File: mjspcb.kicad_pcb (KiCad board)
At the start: 2 copper layers, 97.2 x 55.9 mm, 78 parts, among them P1 Batteries, P10 Lipo, P2 serial breakout, P3 I2C breakout, P4 GPS, P5 piezo, P6 BPW34, P7 electrodes, P8 perfboard breakout, P9 reset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

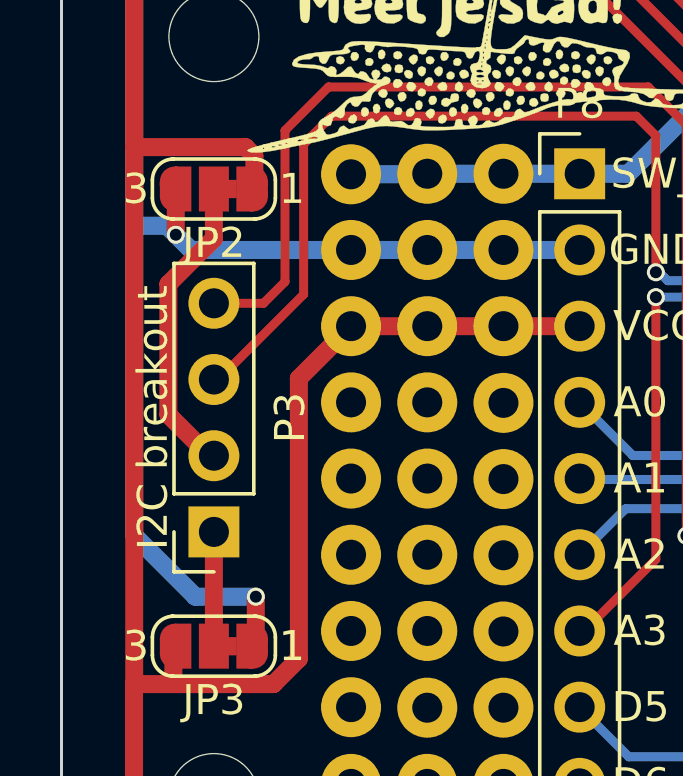
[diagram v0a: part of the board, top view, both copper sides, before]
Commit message: Flip I²C socket
This swaps the pin numbering, to match the Grove pinout. The PCB layout
is also updated to flip the footprint, and move a few traces to make
room for the square pad on the other side.
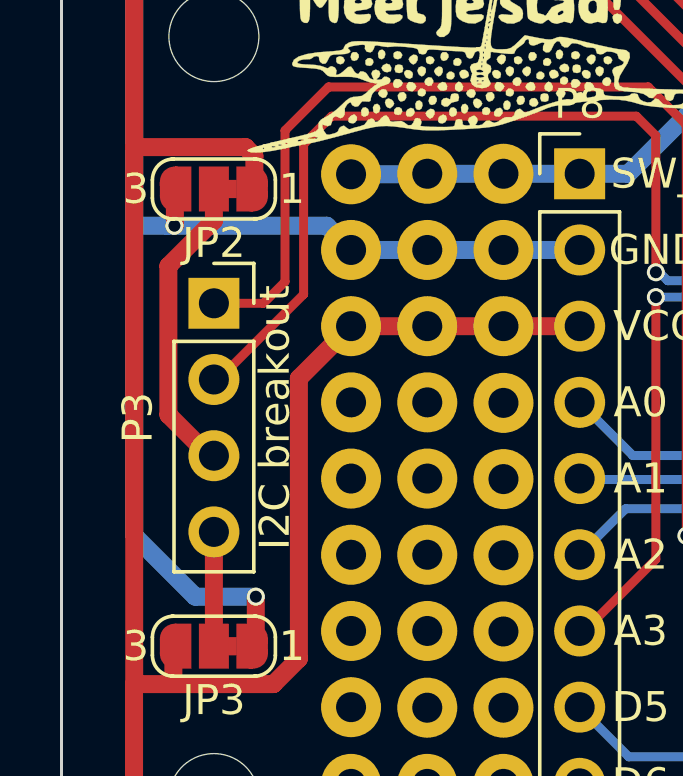
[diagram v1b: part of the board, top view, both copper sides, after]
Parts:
- moved P3 7.62 mm to (139.7, 116.8), turned to 0 degrees
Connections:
- P3 pad 1: Net-(JP3-Pad2) -> SCL
- P3 pad 2: Net-(JP2-Pad2) -> SDA
- P3 pad 3: SDA -> Net-(JP2-Pad2)
- P3 pad 4: SCL -> Net-(JP3-Pad2)
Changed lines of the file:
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@@
     (thickness 1.6)
     (drawings 35)
-    (tracks 533)
+    (tracks 534)
     (zones 0)
     (modules 78)
@@
     (add_net VIN)
   )
+  (module Connector_PinSocket_2.54mm:PinSocket_1x04_P2.54mm_Vertical (layer F.Cu)
+    (at 139.7 116.84)
+    (descr "Through hole straight socket strip, 1x04, 2.54mm pitch, single row (from Kicad 4.0.7), script generated")
+    (tags "Through hole socket strip THT 1x04 2.54mm single row")
+    (fp_text reference P3 (at -2.54 3.81 90) (layer F.SilkS)
+      (effects (font (size 1 1) (thickness 0.15)))
+    )
+    (fp_text value "I2C breakout" (at 2.032 3.81 90) (layer F.SilkS)
+      (effects (font (size 1 1) (thickness 0.15)))
+    )
+    (fp_line (start -1.27 -1.27) (end 0.635 -1.27) (layer F.Fab) (width 0.1))
+    (fp_line (start 0.635 -1.27) (end 1.27 -0.635) (layer F.Fab) (width 0.1))
+    (fp_line (start 1.27 -0.635) (end 1.27 8.89) (layer F.Fab) (width 0.1))
+    (fp_line (start 1.27 8.89) (end -1.27 8.89) (layer F.Fab) (width 0.1))
+    (fp_line (start -1.27 8.89) (end -1.27 -1.27) (layer F.Fab) (width 0.1))
+    (fp_line (start -1.33 1.27) (end 1.33 1.27) (layer F.SilkS) (width 0.12))
+    (fp_line (start -1.33 1.27) (end -1.33 8.95) (layer F.SilkS) (width 0.12))
+    (fp_line (start -1.33 8.95) (end 1.33 8.95) (layer F.SilkS) (width 0.12))
+    (fp_line (start 1.33 1.27) (end 1.33 8.95) (layer F.SilkS) (width 0.12))
+    (fp_line (start 1.33 -1.33) (end 1.33 0) (layer F.SilkS) (width 0.12))
+    (fp_line (start 0 -1.33) (end 1.33 -1.33) (layer F.SilkS) (width 0.12))
+    (fp_line (start -1.8 -1.8) (end 1.75 -1.8) (layer F.CrtYd) (width 0.05))
+    (fp_line (start 1.75 -1.8) (end 1.75 9.4) (layer F.CrtYd) (width 0.05))
+    (fp_line (start 1.75 9.4) (end -1.8 9.4) (layer F.CrtYd) (width 0.05))
+    (fp_line (start -1.8 9.4) (end -1.8 -1.8) (layer F.CrtYd) (width 0.05))
+    (fp_text user %R (at 0 3.81 90) (layer F.Fab)
+      (effects (font (size 1 1) (thickness 0.15)))
+    )
+    (pad 1 thru_hole rect (at 0 0) (size 1.7 1.7) (drill 1) (layers *.Cu *.Mask)
+      (net 11 SCL))
+    (pad 2 thru_hole oval (at 0 2.54) (size 1.7 1.7) (drill 1) (layers *.Cu *.Mask)
+      (net 10 SDA))
+    (pad 3 thru_hole oval (at 0 5.08) (size 1.7 1.7) (drill 1) (layers *.Cu *.Mask)
+      (net 42 "Net-(JP2-Pad2)"))
+    (pad 4 thru_hole oval (at 0 7.62) (size 1.7 1.7) (drill 1) (layers *.Cu *.Mask)
+      (net 43 "Net-(JP3-Pad2)"))
+    (model ${KISYS3DMOD}/Connector_PinSocket_2.54mm.3dshapes/PinSocket_1x04_P2.54mm_Vertical.wrl
+      (at (xyz 0 0 0))
+      (scale (xyz 1 1 1))
+      (rotate (xyz 0 0 0))
+    )
+  )
   (module meetjestad:SolderJumper-3_P1.3mm_Bridged12_RoundedPad1.0x1.5mm_NumberLabels (layer F.Cu)
     (at 139.7 128.27 180)
@@
     )
   )
-  (module Connector_PinSocket_2.54mm:PinSocket_1x04_P2.54mm_Vertical (layer F.Cu)
-    (at 139.7 124.46 180)
-    (descr "Through hole straight socket strip, 1x04, 2.54mm pitch, single row (from Kicad 4.0.7), script generated")
-    (tags "Through hole socket strip THT 1x04 2.54mm single row")
-    (fp_text reference P3 (at -2.54 3.81 270) (layer F.SilkS)
-      (effects (font (size 1 1) (thickness 0.15)))
-    )
-    (fp_text value "I2C breakout" (at 2.032 3.81 270) (layer F.SilkS)
-      (effects (font (size 1 1) (thickness 0.15)))
-    )
-    (fp_line (start -1.27 -1.27) (end 0.635 -1.27) (layer F.Fab) (width 0.1))
-    (fp_line (start 0.635 -1.27) (end 1.27 -0.635) (layer F.Fab) (width 0.1))
-    (fp_line (start 1.27 -0.635) (end 1.27 8.89) (layer F.Fab) (width 0.1))
-    (fp_line (start 1.27 8.89) (end -1.27 8.89) (layer F.Fab) (width 0.1))
-    (fp_line (start -1.27 8.89) (end -1.27 -1.27) (layer F.Fab) (width 0.1))
-    (fp_line (start -1.33 1.27) (end 1.33 1.27) (layer F.SilkS) (width 0.12))
-    (fp_line (start -1.33 1.27) (end -1.33 8.95) (layer F.SilkS) (width 0.12))
-    (fp_line (start -1.33 8.95) (end 1.33 8.95) (layer F.SilkS) (width 0.12))
-    (fp_line (start 1.33 1.27) (end 1.33 8.95) (layer F.SilkS) (width 0.12))
-    (fp_line (start 1.33 -1.33) (end 1.33 0) (layer F.SilkS) (width 0.12))
-    (fp_line (start 0 -1.33) (end 1.33 -1.33) (layer F.SilkS) (width 0.12))
-    (fp_line (start -1.8 -1.8) (end 1.75 -1.8) (layer F.CrtYd) (width 0.05))
-    (fp_line (start 1.75 -1.8) (end 1.75 9.4) (layer F.CrtYd) (width 0.05))
-    (fp_line (start 1.75 9.4) (end -1.8 9.4) (layer F.CrtYd) (width 0.05))
-    (fp_line (start -1.8 9.4) (end -1.8 -1.8) (layer F.CrtYd) (width 0.05))
-    (fp_text user %R (at 0 3.81 270) (layer F.Fab)
-      (effects (font (size 1 1) (thickness 0.15)))
-    )
-    (pad 1 thru_hole rect (at 0 0 180) (size 1.7 1.7) (drill 1) (layers *.Cu *.Mask)
-      (net 43 "Net-(JP3-Pad2)"))
-    (pad 2 thru_hole oval (at 0 2.54 180) (size 1.7 1.7) (drill 1) (layers *.Cu *.Mask)
-      (net 42 "Net-(JP2-Pad2)"))
-    (pad 3 thru_hole oval (at 0 5.08 180) (size 1.7 1.7) (drill 1) (layers *.Cu *.Mask)
-      (net 10 SDA))
-    (pad 4 thru_hole oval (at 0 7.62 180) (size 1.7 1.7) (drill 1) (layers *.Cu *.Mask)
-      (net 11 SCL))
-    (model ${KISYS3DMOD}/Connector_PinSocket_2.54mm.3dshapes/PinSocket_1x04_P2.54mm_Vertical.wrl
-      (at (xyz 0 0 0))
-      (scale (xyz 1 1 1))
-      (rotate (xyz 0 0 0))
-    )
-  )
   (module Connector_JST:JST_PH_S3B-PH-K_1x03_P2.00mm_Horizontal (layer F.Cu)
     (at 170.21302 106.934 180)
@@
   (segment (start 187.833 120.61) (end 185.46 120.61) (width 0.6) (layer B.Cu) (net 2) (status 10))
   (segment (start 137.045157 105.524843) (end 137.045157 114.173) (width 0.6) (layer B.Cu) (net 3))
-  (segment (start 138.43 114.554) (end 138.130001 114.254001) (width 0.6) (layer B.Cu) (net 3))
-  (segment (start 138.130001 114.254001) (end 137.126158 114.254001) (width 0.6) (layer B.Cu) (net 3))
-  (segment (start 137.126158 114.254001) (end 137.045157 114.173) (width 0.6) (layer B.Cu) (net 3))
-  (segment (start 138.43 114.554) (end 138.43 113.11) (width 0.6) (layer F.Cu) (net 3) (status 20))
-  (segment (start 138.43 113.11) (end 138.35 113.03) (width 0.6) (layer F.Cu) (net 3) (status 30))
-  (segment (start 144.272 115.062) (end 138.938 115.062) (width 0.6) (layer B.Cu) (net 3) (status 10))
-  (segment (start 138.938 115.062) (end 138.43 114.554) (width 0.6) (layer B.Cu) (net 3))
-  (via (at 138.43 114.554) (size 0.6) (drill 0.4) (layers F.Cu B.Cu) (net 3))
-  (segment (start 138.190038 112.870038) (end 138.35 113.03) (width 0.6) (layer F.Cu) (net 3) (status 30))
   (segment (start 187.96 103.251) (end 185.42 103.251) (width 0.6) (layer B.Cu) (net 3) (status 30))
   (segment (start 187.96 102.87) (end 187.806377 102.716377) (width 0.6) (layer B.Cu) (net 3) (status 30))
@@
   (segment (start 189.357 116.586) (end 193.04 116.586) (width 0.6) (layer B.Cu) (net 3) (status 20))
   (segment (start 187.833 118.11) (end 189.357 116.586) (width 0.6) (layer B.Cu) (net 3) (status 10))
+  (segment (start 138.190038 112.870038) (end 138.35 113.03) (width 0.6) (layer F.Cu) (net 3) (status 30))
+  (segment (start 137.126158 114.254001) (end 137.045157 114.173) (width 0.6) (layer B.Cu) (net 3))
+  (segment (start 138.130001 114.254001) (end 137.126158 114.254001) (width 0.6) (layer B.Cu) (net 3))
+  (segment (start 138.43 113.11) (end 138.35 113.03) (width 0.6) (layer F.Cu) (net 3) (status 30))
+  (segment (start 143.464001 114.254001) (end 144.272 115.062) (width 0.6) (layer B.Cu) (net 3))
+  (segment (start 138.4 113.03) (end 138.4 114.238002) (width 0.6) (layer F.Cu) (net 3))
+  (segment (start 138.4 114.238002) (end 138.384001 114.254001) (width 0.6) (layer F.Cu) (net 3))
+  (segment (start 138.130001 114.254001) (end 138.384001 114.254001) (width 0.6) (layer B.Cu) (net 3))
+  (via (at 138.384001 114.254001) (size 0.6) (drill 0.4) (layers F.Cu B.Cu) (net 3))
+  (segment (start 138.384001 114.254001) (end 143.464001 114.254001) (width 0.6) (layer B.Cu) (net 3))
   (segment (start 195.068647 104.945557) (end 190.794204 109.22) (width 0.3) (layer F.Cu) (net 4) (status 20))
   (segment (start 198.12 103.4034) (end 196.577843 104.945557) (width 0.3) (layer F.Cu) (net 4) (status 10))
@@
   (segment (start 194.564 117.856) (end 193.04 117.856) (width 0.6) (layer F.Cu) (net 41) (status 20))
   (segment (start 197.104 115.316) (end 194.564 117.856) (width 0.6) (layer F.Cu) (net 41) (status 10))
-  (segment (start 138.18399 116.19701) (end 139.7 114.681) (width 0.6) (layer F.Cu) (net 42))
-  (segment (start 139.7 114.681) (end 139.7 113.03) (width 0.6) (layer F.Cu) (net 42) (status 20))
-  (segment (start 139.7 121.92) (end 139.5476 121.92) (width 0.6) (layer F.Cu) (net 42) (status 30))
-  (segment (start 139.5476 121.92) (end 138.18399 120.55639) (width 0.6) (layer F.Cu) (net 42) (status 10))
-  (segment (start 138.18399 120.55639) (end 138.18399 116.19701) (width 0.6) (layer F.Cu) (net 42))
+  (segment (start 139.7 114.081002) (end 139.7 113.03) (width 0.6) (layer F.Cu) (net 42))
+  (segment (start 138.18399 115.597012) (end 139.7 114.081002) (width 0.6) (layer F.Cu) (net 42))
+  (segment (start 138.18399 120.55639) (end 138.18399 115.597012) (width 0.6) (layer F.Cu) (net 42))
+  (segment (start 139.7 121.92) (end 139.5476 121.92) (width 0.6) (layer F.Cu) (net 42))
+  (segment (start 139.5476 121.92) (end 138.18399 120.55639) (width 0.6) (layer F.Cu) (net 42))
   (segment (start 139.7 124.46) (end 139.7 128.27) (width 0.6) (layer F.Cu) (net 43) (status 30))
   (zone (net 3) (net_name GND) (layer B.Cu) (hatch edge 0.508)
